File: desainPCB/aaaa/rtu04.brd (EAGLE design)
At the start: 78.7 x 77.1 mm, 18 parts, among them M1 ARDUINO-PRO-MINI-5.0V, X1 JST-XH-02-PIN-LONG-PAD

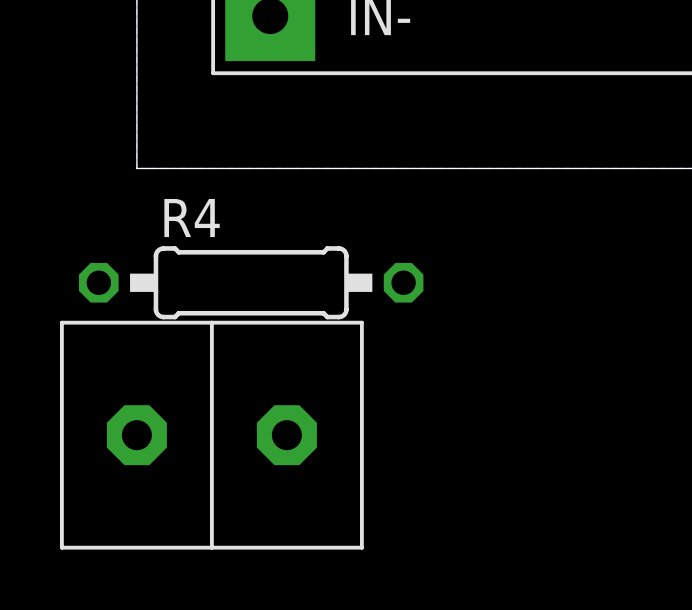
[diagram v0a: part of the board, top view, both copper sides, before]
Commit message: fix calib for strain 2.0
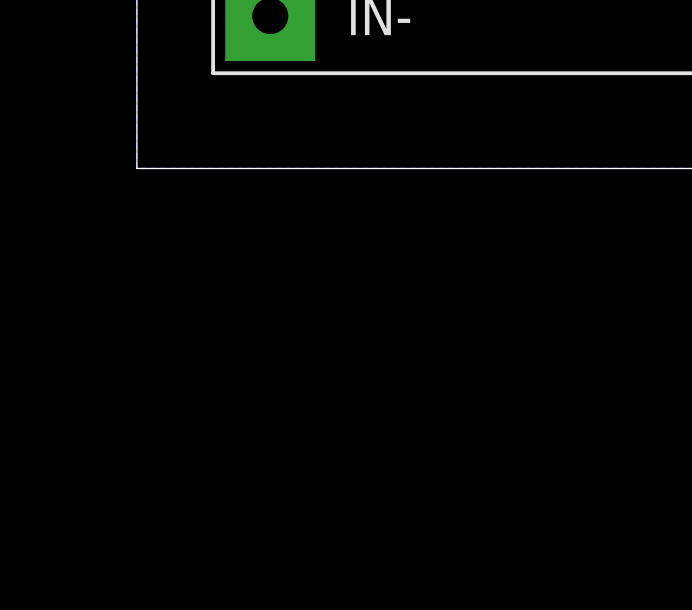
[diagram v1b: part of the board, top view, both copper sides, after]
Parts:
- removed R4: (no value), rcl:0207/10
- removed U$4: DBCONN-1X2, Terminal Block Connector:DBCONN-1X2
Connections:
- net A+: no longer R4.2
- net A-: no longer U$4.P1
- net E-: no longer R4.1, U$4.P0
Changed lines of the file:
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@@
 <attribute name="VALUE" x="2.413" y="45.339" size="1.27" layer="27" ratio="10" rot="R270"/>
 </element>
-<element name="R4" library="rcl" library_urn="urn:adsk.eagle:library:334" package="0207/10" package3d_urn="urn:adsk.eagle:package:23491/2" value="" x="3.81" y="-3.81" smashed="yes">
-<attribute name="NAME" x="0.762" y="-2.286" size="1.27" layer="25" ratio="10"/>
-<attribute name="POPULARITY" value="81" x="3.81" y="-3.81" size="1.778" layer="27" display="off"/>
-<attribute name="SPICEPREFIX" value="R" x="3.81" y="-3.81" size="1.778" layer="27" display="off"/>
-<attribute name="VALUE" x="1.5494" y="-4.445" size="1.27" layer="27" ratio="10"/>
-</element>
-<element name="U$4" library="Terminal Block Connector" package="DBCONN-1X2" value="DBCONN-1X2" x="2.54" y="-8.89" smashed="yes"/>
 </elements>
 <signals>
@@
 <wire x1="15.24" y1="68.58" x2="31.75" y2="52.07" width="0.508" layer="16"/>
 <wire x1="31.75" y1="52.07" x2="36.63" y2="52.07" width="0.508" layer="16"/>
-<contactref element="R4" pad="1"/>
-<contactref element="U$4" pad="P0"/>
-<wire x1="-1.27" y1="-3.81" x2="36.63" y2="52.07" width="0" layer="19" extent="1-1"/>
-<wire x1="0" y1="-8.89" x2="-1.27" y2="-3.81" width="0" layer="19" extent="1-1"/>
 </signal>
 <signal name="A-">
@@
 <wire x1="33.02" y1="68.58" x2="33.02" y2="58.22" width="0.508" layer="16"/>
 <wire x1="36.63" y1="54.61" x2="33.02" y2="58.22" width="0.508" layer="16"/>
-<contactref element="U$4" pad="P1"/>
-<wire x1="5" y1="-8.89" x2="36.63" y2="54.61" width="0" layer="19" extent="1-1"/>
 </signal>
 <signal name="A+">
@@
 <wire x1="32.82" y1="60.96" x2="20.32" y2="60.96" width="0.508" layer="1"/>
 <wire x1="32.82" y1="60.96" x2="36.63" y2="57.15" width="0.508" layer="1"/>
-<contactref element="R4" pad="2"/>
-<wire x1="8.89" y1="-3.81" x2="36.63" y2="57.15" width="0" layer="19" extent="1-1"/>
 </signal>
 <signal name="A1">
